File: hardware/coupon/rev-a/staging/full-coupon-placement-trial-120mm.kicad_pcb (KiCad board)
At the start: 6 copper layers, 120 x 32.5 mm, 497 parts, among them J1 USB4505-03-0-A, J2 S2B-PH-SM4-TB, Q1 DMP2066LSN-7, Q10 DMP2066LSN-7, Q11 DMP2066LSN-7, Q12 DMP2066LSN-7, Q13 DMP2066LSN-7, Q14 DMP2066LSN-7, Q15 DMP2066LSN-7, Q16 DMP2066LSN-7, Q17 2N7002K-7, Q18 2N7002K-7, Q19 2N7002K-7, Q2 DMP2066LSN-7, Q20 2N7002K-7, Q21 2N7002K-7, Q22 2N7002K-7, Q23 2N7002K-7, Q24 2N7002K-7, Q25 2N7002K-7, Q26 2N7002K-7, Q27 2N7002K-7, Q28 2N7002K-7, Q29 2N7002K-7, Q3 DMP2066LSN-7, Q30 2N7002K-7, Q31 2N7002K-7, Q32 2N7002K-7, Q4 DMP2066LSN-7, Q5 DMP2066LSN-7, Q6 DMP2066LSN-7, Q7 DMP2066LSN-7, Q8 DMP2066LSN-7, Q9 DMP2066LSN-7, SW1 EVQP7J01P, SW2 JS202011JCQN, U1 TLC59581RTQT, U11 SN74LVC1G04DBVR, U17 SN74LVC1G11DBVR, U2 74HC4514PW,118, U23 SN74LVC1G06DBVR, U24 SN74LVC2G17DBVR, U25 SN74LVC2G17DBVR, U29 TPS70933DBVR, U3 ESP32-S3-WROOM-1U-N16R8, U31 TUSB320LAIRWBR, U32 TS3USB31ERSER, U33 TPD4E05U06DQAR, U34 TPS3808G01DBVR, U35 MAX17048G+T10, U36 TPS631000DRLR, U37 TPS63020DSJT, U38 2.5V shunt, U39 TMP390A2DRLR, U40 SN74AUP1G125DBVR, U41 BQ24074RGTR, U42 SN74AUP1G125DBVR, U43 SN74AUP1G125DBVR, U44 TPS259474ARPWR, U45 TPS259474ARPWR, U46 TCA9517ADGKR, U47 TPS3823A-33DBVR, U48 SN74LVC1G04DSFR, U49 SN74LVC1G74RSER, U50 SN74LVC1G74RSER, U51 SN74LVC1G11DRYR, U52 SN74LVC1G08DSFR, U53 TLV6700DSER, U54 SN74LVC2G00DCUR, U55 SN74LVC2G08DCUR

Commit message: Place and route local charger ILIM reference loop
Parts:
- moved TP33 111.0 mm to (4.00, 30.8)
- moved Q29 95.8 mm to (22.2, 29.2)
- moved Q31 74.8 mm to (101.0, 30.0)
- moved R93 56.4 mm to (117.2, 28.2)
- moved TP9 13.3 mm to (31.3, 31.5)
- moved U35 12.0 mm to (117.0, 30.4)
- moved Q32 8.00 mm to (109.0, 30.0)
- moved L1 4.07 mm to (105.0, 30.4)
- moved Q30 4.00 mm to (26.2, 29.2)
- moved R94 2.50 mm to (63.2, 11.8)
- moved R95 2.50 mm to (65.8, 11.8)
- moved TH1 2.50 mm to (68.1, 11.9)
- moved TP34 2.00 mm to (6.00, 30.8)
- moved TP5 2.00 mm to (12.0, 30.8)
- moved TP6 2.00 mm to (14.0, 30.8)
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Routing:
- net GND: track 0.00 -> 11.5 mm, vias 0 -> 3
- net CHARGER_ILIM: track 0.00 -> 3.82 mm
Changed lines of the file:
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@@
 	(footprint "rgb-badge-coupon:L_Murata_DFE252012P"
 		(layer "B.Cu")
-		(at 109 29.625 180)
+		(at 105 30.375 180)
 		(descr "Murata DFE252012P 2.8 x 2.0 mm recommended lands, 1.2 mm inner gap; SPDX-License-Identifier: CERN-OHL-S-2.0")
 		(property "Reference" "L1"
@@
 	(footprint "rgb-badge-coupon:SOT23_Diodes_2N7002K"
 		(layer "B.Cu")
-		(at 118 28.75 180)
+		(at 22.25 29.25 180)
 		(descr "Diodes Incorporated SOT23 suggested pad layout for 2N7002K; SPDX-License-Identifier: CERN-OHL-S-2.0")
 		(property "Reference" "Q29"
@@
 	(footprint "rgb-badge-coupon:SOT23_Diodes_2N7002K"
 		(layer "B.Cu")
-		(at 22.25 29.25 180)
+		(at 26.25 29.25 180)
 		(descr "Diodes Incorporated SOT23 suggested pad layout for 2N7002K; SPDX-License-Identifier: CERN-OHL-S-2.0")
 		(property "Reference" "Q30"
@@
 	(footprint "rgb-badge-coupon:SOT23_Diodes_2N7002K"
 		(layer "B.Cu")
-		(at 26.25 29.25 180)
+		(at 101 30 180)
 		(descr "Diodes Incorporated SOT23 suggested pad layout for 2N7002K; SPDX-License-Identifier: CERN-OHL-S-2.0")
 		(property "Reference" "Q31"
@@
 	(footprint "rgb-badge-coupon:SOT23_Diodes_2N7002K"
 		(layer "B.Cu")
-		(at 101 30 180)
+		(at 109 30 180)
 		(descr "Diodes Incorporated SOT23 suggested pad layout for 2N7002K; SPDX-License-Identifier: CERN-OHL-S-2.0")
 		(property "Reference" "Q32"
@@
 	(footprint "rgb-badge-coupon:R_Panasonic_ERA2_0402"
 		(layer "B.Cu")
-		(at 63.25 11.875 180)
+		(at 117.25 28.25 180)
 		(descr "Manufacturer range-based reflow land pattern; SPDX-License-Identifier: CERN-OHL-S-2.0")
 		(property "Reference" "R93"
@@
 	(footprint "rgb-badge-coupon:R_Panasonic_ERJ2_0402"
 		(layer "B.Cu")
-		(at 65.75 11.75 180)
+		(at 63.25 11.75 180)
 		(descr "Manufacturer range-based reflow land pattern; SPDX-License-Identifier: CERN-OHL-S-2.0")
 		(property "Reference" "R94"
@@
 	(footprint "rgb-badge-coupon:R_Panasonic_ERJ2_0402"
 		(layer "B.Cu")
-		(at 68.25 11.75 180)
+		(at 65.75 11.75 180)
 		(descr "Manufacturer range-based reflow land pattern; SPDX-License-Identifier: CERN-OHL-S-2.0")
 		(property "Reference" "R95"
@@
 	(footprint "rgb-badge-coupon:NTC_Murata_NCU15_0402"
 		(layer "B.Cu")
-		(at 70.625 11.875 180)
+		(at 68.125 11.875 180)
 		(descr "Murata NCU15 1005 NTC, reflow land a=0.4 b=0.45 c=0.5 mm; SPDX-License-Identifier: CERN-OHL-S-2.0")
 		(property "Reference" "TH1"
@@
 	(footprint "rgb-badge-coupon:TestPoint_Pad_D1.0mm"
 		(layer "B.Cu")
-		(at 115.001261 30.5 180)
+		(at 4.001261 30.75 180)
 		(descr "Bare 1.0 mm copper probe pad; no purchased component or solder paste. SPDX-License-Identifier: CERN-OHL-S-2.0")
 		(property "Reference" "TP33"
@@
 	(footprint "rgb-badge-coupon:TestPoint_Pad_D1.0mm"
 		(layer "B.Cu")
-		(at 4.001261 30.75 180)
+		(at 6.001261 30.75 180)
 		(descr "Bare 1.0 mm copper probe pad; no purchased component or solder paste. SPDX-License-Identifier: CERN-OHL-S-2.0")
 		(property "Reference" "TP34"
@@
 	(footprint "rgb-badge-coupon:TestPoint_Pad_D1.0mm"
 		(layer "B.Cu")
-		(at 6.001261 30.75 180)
+		(at 8.001261 30.75 180)
 		(descr "Bare 1.0 mm copper probe pad; no purchased component or solder paste. SPDX-License-Identifier: CERN-OHL-S-2.0")
 		(property "Reference" "TP35"
@@
 	(footprint "rgb-badge-coupon:TestPoint_Pad_D1.0mm"
 		(layer "B.Cu")
-		(at 7.851261 30.75 180)
+		(at 9.851261 30.75 180)
 		(descr "Bare 1.0 mm copper probe pad; no purchased component or solder paste. SPDX-License-Identifier: CERN-OHL-S-2.0")
 		(property "Reference" "TP4"
@@
 	(footprint "rgb-badge-coupon:TestPoint_Pad_D1.0mm"
 		(layer "B.Cu")
-		(at 10.001261 30.75 180)
+		(at 12.001261 30.75 180)
 		(descr "Bare 1.0 mm copper probe pad; no purchased component or solder paste. SPDX-License-Identifier: CERN-OHL-S-2.0")
 		(property "Reference" "TP5"
@@
 	(footprint "rgb-badge-coupon:TestPoint_Pad_D1.0mm"
 		(layer "B.Cu")
-		(at 12.001261 30.75 180)
+		(at 14.001261 30.75 180)
 		(descr "Bare 1.0 mm copper probe pad; no purchased component or solder paste. SPDX-License-Identifier: CERN-OHL-S-2.0")
 		(property "Reference" "TP6"
@@
 	(footprint "rgb-badge-coupon:TestPoint_Pad_D1.0mm"
 		(layer "B.Cu")
-		(at 14.001261 30.75 180)
+		(at 16.001261 30.75 180)
 		(descr "Bare 1.0 mm copper probe pad; no purchased component or solder paste. SPDX-License-Identifier: CERN-OHL-S-2.0")
 		(property "Reference" "TP7"
@@
 	(footprint "rgb-badge-coupon:TestPoint_Pad_D1.0mm"
 		(layer "B.Cu")
-		(at 16.001261 30.75 180)
+		(at 18.001261 30.75 180)
 		(descr "Bare 1.0 mm copper probe pad; no purchased component or solder paste. SPDX-License-Identifier: CERN-OHL-S-2.0")
 		(property "Reference" "TP8"
@@
 	(footprint "rgb-badge-coupon:TestPoint_Pad_D1.0mm"
 		(layer "B.Cu")
-		(at 18.001261 30.75 180)
+		(at 31.251261 31.5 180)
 		(descr "Bare 1.0 mm copper probe pad; no purchased component or solder paste. SPDX-License-Identifier: CERN-OHL-S-2.0")
 		(property "Reference" "TP9"
@@
 	(footprint "rgb-badge-coupon:TDFN_Maxim_T822-3_2x2mm_P0.5mm_EP0.7x1.38mm"
 		(layer "B.Cu")
-		(at 105 30.375 180)
+		(at 117 30.375 180)
 		(descr "Maxim T822+3 2 x 2 mm TDFN-EP land pattern 90-0065 for MAX17048G+T10; full-area exposed-pad paste is provisional for assembler DFM; SPDX-License-Identifier: CERN-OHL-S-2.0")
 		(property "Reference" "U35"
@@
 	)
 	(segment
+		(start 110.5 24.5)
+		(end 110.5 25.55)
+		(width 0.2)
+		(layer "In3.Cu")
+		(net "GND")
+	)
+	(segment
+		(start 110.5 25.55)
+		(end 112.45 27.5)
+		(width 0.2)
+		(layer "In3.Cu")
+		(net "GND")
+	)
+	(segment
 		(start 110.55 16.8)
 		(end 110.55 16)
@@
 	)
 	(segment
+		(start 112.35 24.5)
+		(end 110.5 24.5)
+		(width 0.2)
+		(layer "B.Cu")
+		(net "GND")
+	)
+	(segment
+		(start 112.45 27.5)
+		(end 112.45 28.75)
+		(width 0.2)
+		(layer "B.Cu")
+		(net "GND")
+	)
+	(segment
+		(start 113.2 28.25)
+		(end 112.45 27.5)
+		(width 0.2)
+		(layer "In3.Cu")
+		(net "GND")
+	)
+	(segment
 		(start 113.25 18.65)
 		(end 112.2 18.65)
@@
 	)
 	(segment
+		(start 115.15 26)
+		(end 116 26)
+		(width 0.2)
+		(layer "B.Cu")
+		(net "CHARGER_ILIM")
+	)
+	(segment
+		(start 115.75 28.25)
+		(end 113.2 28.25)
+		(width 0.2)
+		(layer "In3.Cu")
+		(net "GND")
+	)
+	(segment
+		(start 116 26)
+		(end 117.75 27.75)
+		(width 0.2)
+		(layer "B.Cu")
+		(net "CHARGER_ILIM")
+	)
+	(segment
+		(start 116.75 28.25)
+		(end 115.75 28.25)
+		(width 0.2)
+		(layer "B.Cu")
+		(net "GND")
+	)
+	(segment
+		(start 117.75 27.75)
+		(end 117.75 28.25)
+		(width 0.2)
+		(layer "B.Cu")
+		(net "CHARGER_ILIM")
+	)
+	(segment
 		(start 45.8 0.65)
 		(end 59.45 0.65)
@@
 	)
 	(via
+		(at 110.5 24.5)
+		(size 0.6)
+		(drill 0.3)
+		(layers "F.Cu" "B.Cu")
+		(net "GND")
+	)
+	(via
 		(at 110.55 16.8)
 		(size 0.6)
@@
 	)
 	(via
+		(at 112.45 27.5)
+		(size 0.6)
+		(drill 0.3)
+		(layers "F.Cu" "B.Cu")
+		(net "GND")
+	)
+	(via
 		(at 114.5 27.5)
 		(size 0.6)
@@
 		(net "CHARGER_IN_DRAFT")
 	)
+	(via
+		(at 115.75 28.25)
+		(size 0.6)
+		(drill 0.3)
+		(layers "F.Cu" "B.Cu")
+		(net "GND")
+	)
 	(embedded_fonts no)

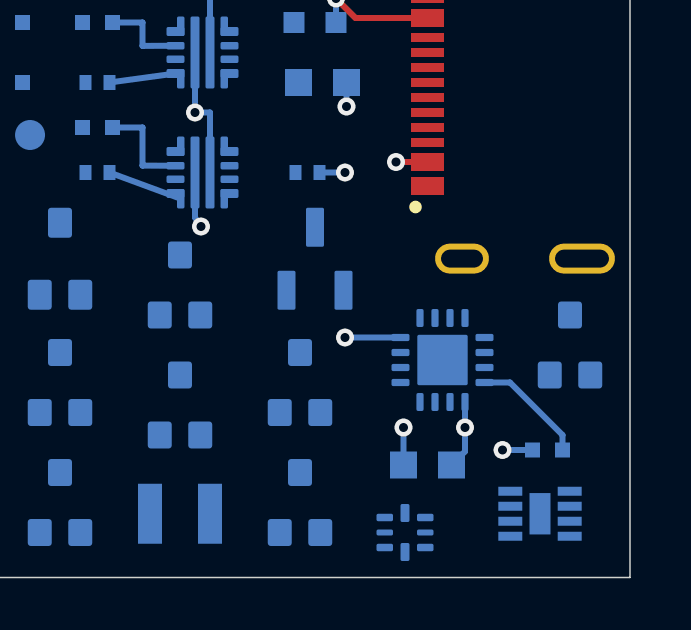
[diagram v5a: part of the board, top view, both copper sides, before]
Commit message: Connect remaining charger ground pads in placement study
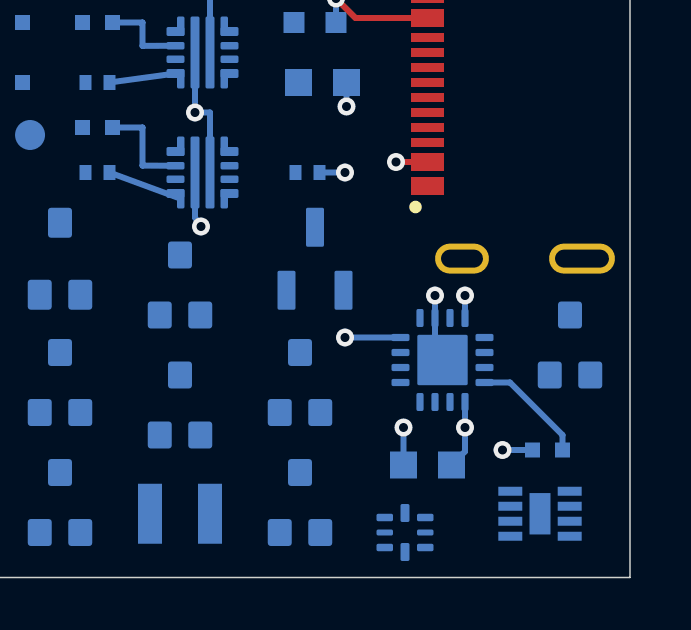
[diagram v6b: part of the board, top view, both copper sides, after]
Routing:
- net GND: track 11.5 -> 21.3 mm, vias 3 -> 5
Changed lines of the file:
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@@
+	)
+	(segment
+		(start 113.5 23.1)
+		(end 110.5 24.5)
+		(width 0.2)
+		(layer "In3.Cu")
+		(net "GND")
+	)
+	(segment
+		(start 113.5 23.85)
+		(end 113.5 23.1)
+		(width 0.2)
+		(layer "B.Cu")
+		(net "GND")
+	)
+	(segment
+		(start 113.5 23.85)
+		(end 113.5 24.6)
+		(width 0.2)
+		(layer "B.Cu")
+		(net "GND")
+	)
+	(segment
+		(start 114.5 23.1)
+		(end 110.5 24.5)
+		(width 0.2)
+		(layer "In3.Cu")
+		(net "GND")
+	)
+	(segment
+		(start 114.5 23.85)
+		(end 114.5 23.1)
+		(width 0.2)
+		(layer "B.Cu")
+		(net "GND")
 	)
 	(segment
@@
 		(size 0.6)
 		(drill 0.3)
+		(layers "F.Cu" "B.Cu")
+		(net "GND")
+	)
+	(via
+		(at 113.5 23.1)
+		(size 0.6)
+		(drill 0.3)
+		(layers "F.Cu" "B.Cu")
+		(net "GND")
+	)
+	(via
+		(at 114.5 23.1)
+		(size 0.6)
+		(drill 0.3)

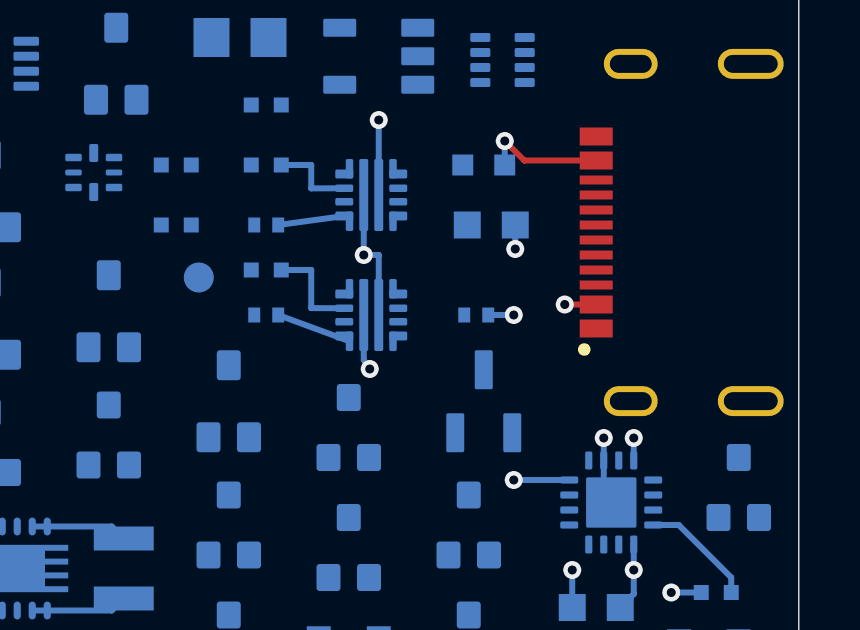
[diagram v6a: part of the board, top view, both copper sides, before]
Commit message: Join charger output capacitor to local ground trial
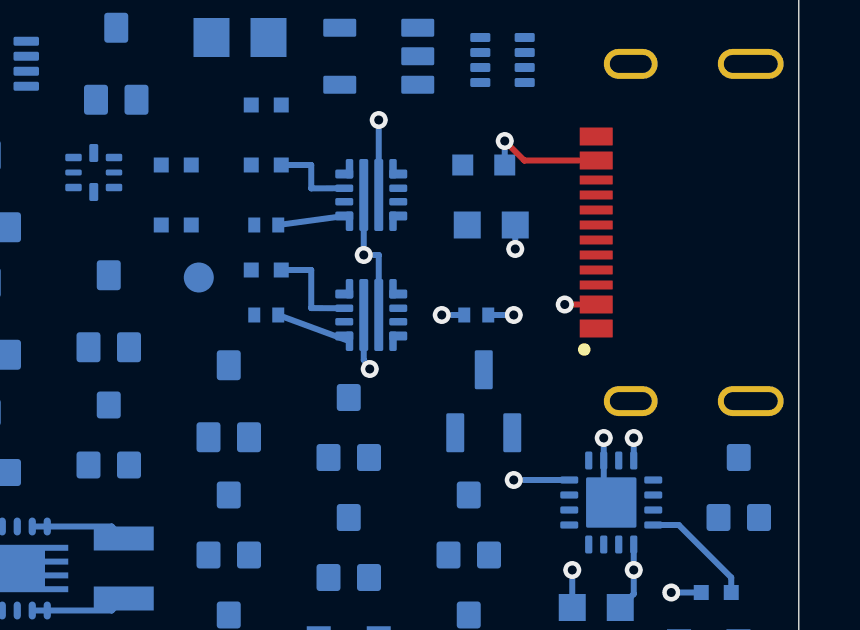
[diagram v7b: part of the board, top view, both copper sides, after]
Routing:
- net GND: track 21.3 -> 28.1 mm, vias 5 -> 6
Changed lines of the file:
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@@
+	)
+	(segment
+		(start 108.1 19)
+		(end 110.5 24.5)
+		(width 0.2)
+		(layer "In3.Cu")
+		(net "GND")
 	)
 	(segment
@@
 		(layer "In4.Cu")
 		(net "CHARGER_IN_DRAFT")
+	)
+	(segment
+		(start 108.85 19)
+		(end 108.1 19)
+		(width 0.2)
+		(layer "B.Cu")
+		(net "GND")
 	)
 	(segment
@@
 	)
 	(via
+		(at 108.1 19)
+		(size 0.6)
+		(drill 0.3)
+		(layers "F.Cu" "B.Cu")
+		(net "GND")
+	)
+	(via

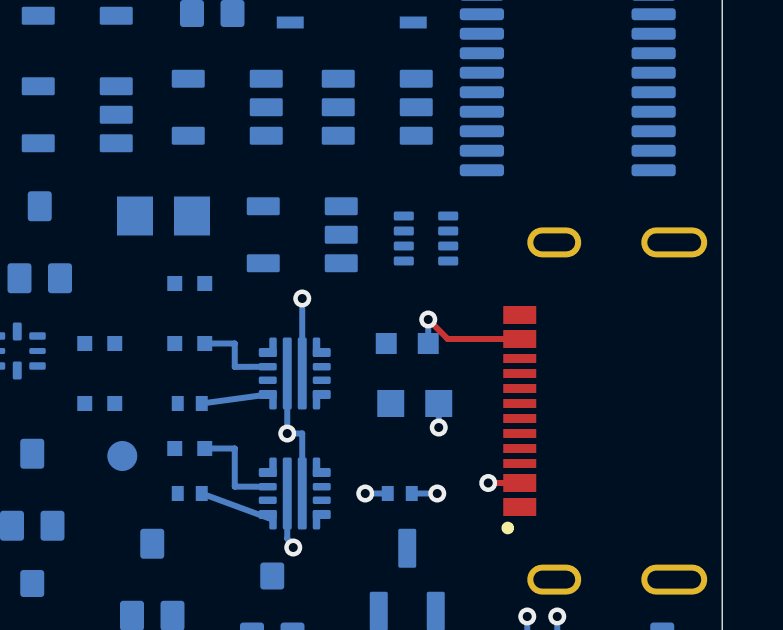
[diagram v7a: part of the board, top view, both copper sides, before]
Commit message: Join USB ground contact to input capacitor in layout trial
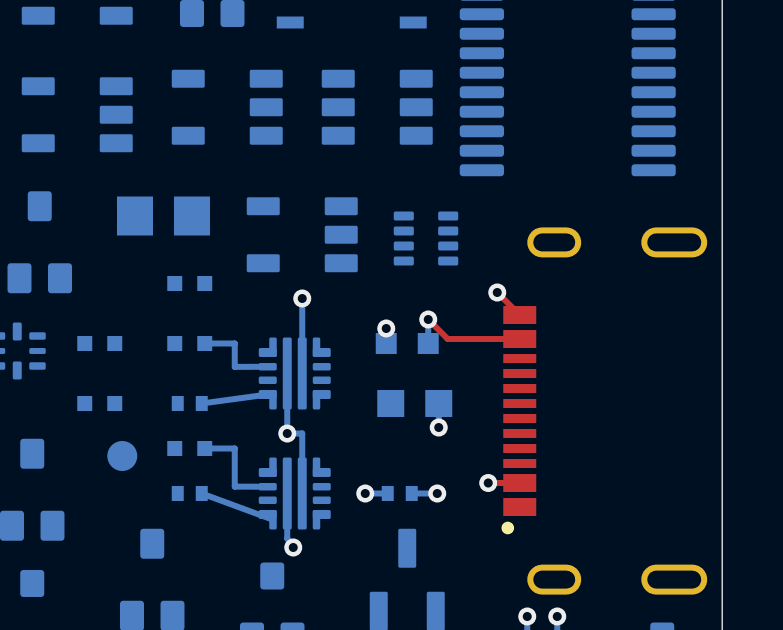
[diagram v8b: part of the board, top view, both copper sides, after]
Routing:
- net GND: track 28.1 -> 35.2 mm, vias 6 -> 8
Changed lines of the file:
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@@
+	)
+	(segment
+		(start 108.8 13.5)
+		(end 110.2 15)
+		(width 0.2)
+		(layer "In3.Cu")
+		(net "GND")
+	)
+	(segment
+		(start 108.8 14)
+		(end 108.8 13.5)
+		(width 0.2)
+		(layer "B.Cu")
+		(net "GND")
 	)
 	(segment
@@
 	)
 	(segment
+		(start 110.2 15)
+		(end 112.5 12.3)
+		(width 0.2)
+		(layer "In3.Cu")
+		(net "GND")
+	)
+	(segment
 		(start 110.35 17)
 		(end 110.55 16.8)
@@
 		(width 0.2)
 		(layer "B.Cu")
+		(net "GND")
+	)
+	(segment
+		(start 112.5 12.3)
+		(end 113.25 13.05)
+		(width 0.2)
+		(layer "F.Cu")
 		(net "GND")
 	)
@@
 	)
 	(via
+		(at 108.8 13.5)
+		(size 0.6)
+		(drill 0.3)
+		(layers "F.Cu" "B.Cu")
+		(net "GND")
+	)
+	(via
 		(at 110.2 13.2)
 		(size 0.6)
@@
 		(size 0.6)
 		(drill 0.3)
+		(layers "F.Cu" "B.Cu")
+		(net "GND")
+	)
+	(via
+		(at 112.5 12.3)
+		(size 0.6)
+		(drill 0.3)
